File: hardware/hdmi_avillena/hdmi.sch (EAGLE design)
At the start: 5 parts

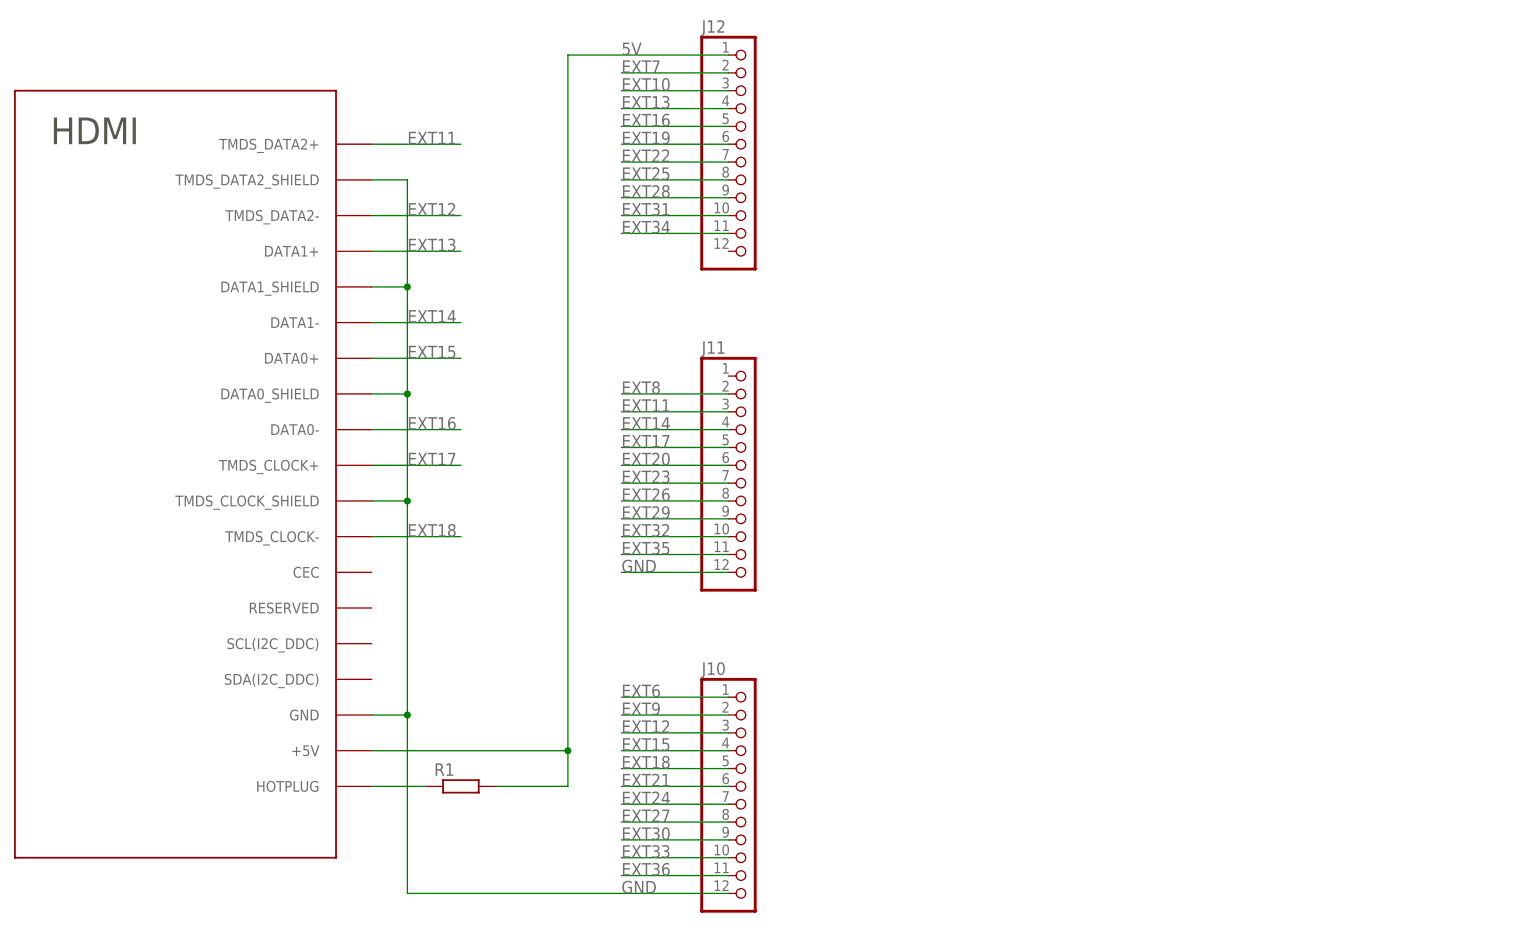
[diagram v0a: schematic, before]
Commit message: 
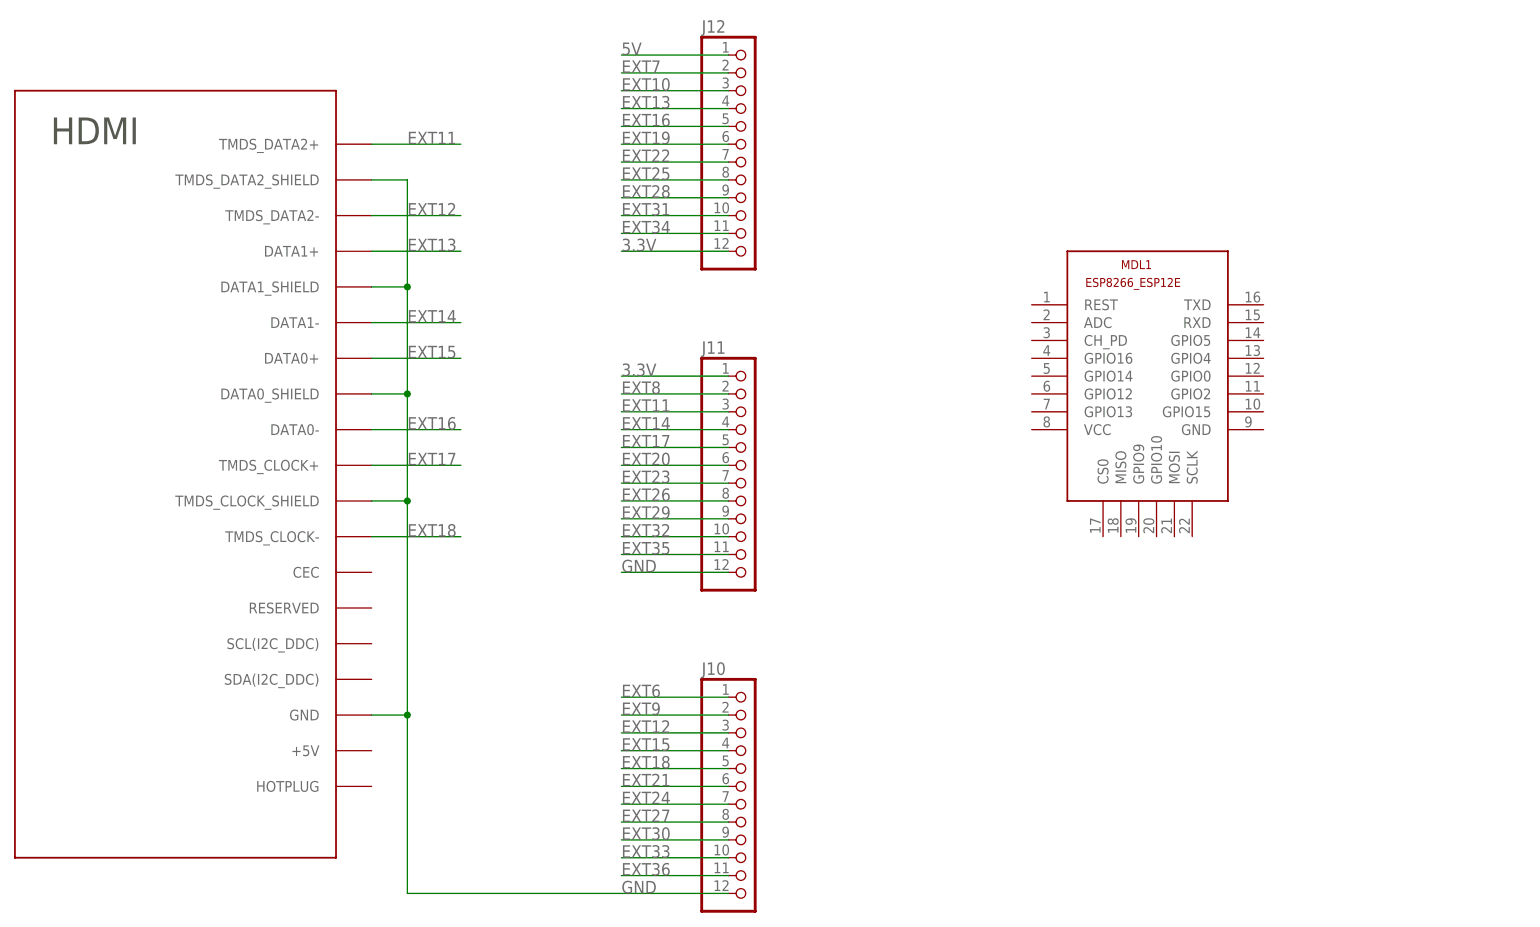
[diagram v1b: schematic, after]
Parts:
- removed R1: (no value), rcl:R-EU_0204/7
- added MDL1: (no value), ESP8266-ESP12E:ESP8266-12EESP8266-ESP12E
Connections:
- removed net N$2: R1.1, U$1.HOTPLUG
- new net 3.3V: J11.1, J12.12
- net 5V: no longer R1.2, U$1.+5V
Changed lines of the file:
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@@
 <part name="J10" library="pinhead" deviceset="PINHD-1X12" device=""/>
 <part name="U$1" library="00_cody" deviceset="HDMI" device=""/>
-<part name="R1" library="rcl" deviceset="R-EU_" device="0204/7"/>
+<part name="MDL1" library="ESP8266-ESP12E" deviceset="ESP8266-12E" device="ESP8266-ESP12E"/>
 </parts>
 <sheets>
@@
 <instance part="J10" gate="G$1" x="27.94" y="-2.54"/>
 <instance part="U$1" gate="G$1" x="-33.02" y="68.58"/>
-<instance part="R1" gate="G$1" x="-12.7" y="-2.54"/>
+<instance part="MDL1" gate="G$1" x="91.44" y="58.42"/>
 </instances>
 <busses>
@@
 </segment>
 </net>
-<net name="5V" class="0">
-<segment>
-<wire x1="2.54" y1="101.6" x2="25.4" y2="101.6" width="0.1524" layer="91"/>
-<label x="10.16" y="101.6" size="1.778" layer="95"/>
-<pinref part="J12" gate="G$1" pin="1"/>
-<pinref part="U$1" gate="G$1" pin="+5V"/>
-<wire x1="-25.4" y1="2.54" x2="2.54" y2="2.54" width="0.1524" layer="91"/>
-<wire x1="2.54" y1="2.54" x2="2.54" y2="101.6" width="0.1524" layer="91"/>
-<pinref part="R1" gate="G$1" pin="2"/>
-<wire x1="-7.62" y1="-2.54" x2="2.54" y2="-2.54" width="0.1524" layer="91"/>
-<wire x1="2.54" y1="-2.54" x2="2.54" y2="2.54" width="0.1524" layer="91"/>
-<junction x="2.54" y="2.54"/>
-</segment>
-</net>
 <net name="EXT6" class="0">
 <segment>
@@
 </segment>
 </net>
-<net name="N$2" class="0">
-<segment>
-<pinref part="U$1" gate="G$1" pin="HOTPLUG"/>
-<pinref part="R1" gate="G$1" pin="1"/>
-<wire x1="-25.4" y1="-2.54" x2="-17.78" y2="-2.54" width="0.1524" layer="91"/>
-</segment>
-</net>
+<net name="5V" class="0">
+<segment>
+<pinref part="J12" gate="G$1" pin="1"/>
+<wire x1="25.4" y1="101.6" x2="10.16" y2="101.6" width="0.1524" layer="91"/>
+<label x="10.16" y="101.6" size="1.778" layer="95"/>
+</segment>
+</net>
+<net name="3.3V" class="0">
+<segment>
+<pinref part="J11" gate="G$1" pin="1"/>
+<wire x1="25.4" y1="55.88" x2="10.16" y2="55.88" width="0.1524" layer="91"/>
+<label x="10.16" y="55.88" size="1.778" layer="95"/>
+</segment>
+<segment>
+<pinref part="J12" gate="G$1" pin="12"/>
+<wire x1="25.4" y1="73.66" x2="10.16" y2="73.66" width="0.1524" layer="91"/>
+<label x="10.16" y="73.66" size="1.778" layer="95"/>
+</segment>
+</net>

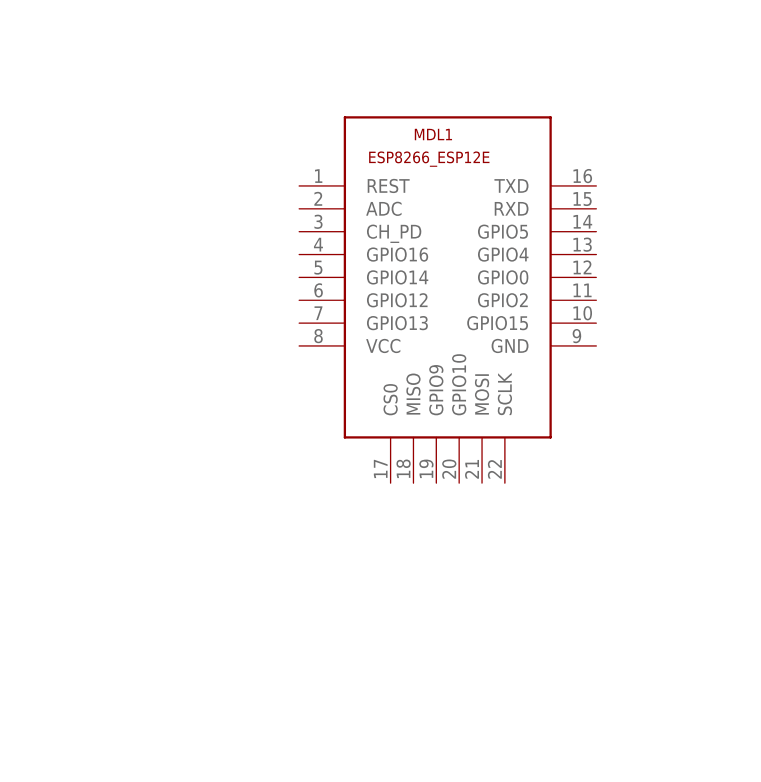
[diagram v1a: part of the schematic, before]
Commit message: 
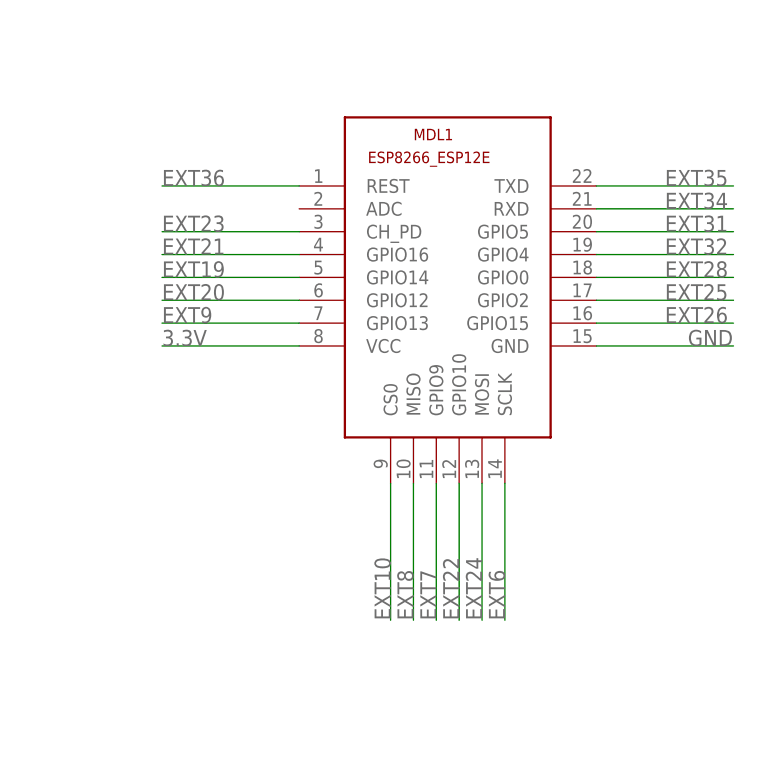
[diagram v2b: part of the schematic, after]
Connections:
- net 3.3V: now also MDL1.VCC
- net EXT10: now also MDL1.CS0
- net EXT19: now also MDL1.GPIO14
- net EXT20: now also MDL1.GPIO12
- net EXT21: now also MDL1.GPIO16
- net EXT22: now also MDL1.GPIO10
- net EXT23: now also MDL1.CH_PD
- net EXT24: now also MDL1.MOSI
- net EXT25: now also MDL1.GPIO2
- net EXT26: now also MDL1.GPIO15
- net EXT28: now also MDL1.GPIO0
- net EXT31: now also MDL1.GPIO5
- net EXT32: now also MDL1.GPIO4
- net EXT34: now also MDL1.RXD
- net EXT35: now also MDL1.TXD
- net EXT36: now also MDL1.REST
- net EXT6: now also MDL1.SCLK
- net EXT7: now also MDL1.GPIO9
- net EXT8: now also MDL1.MISO
- net EXT9: now also MDL1.GPIO13
- net GND: now also MDL1.GND

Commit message: 
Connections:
- removed net EXT36: J10.11, MDL1.REST
- net EXT33: now also MDL1.REST
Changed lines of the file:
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@@
 <grid distance="0.1" unitdist="inch" unit="inch" style="lines" multiple="1" display="no" altdistance="0.01" altunitdist="inch" altunit="inch"/>
 <layers>
-<layer number="1" name="Top" color="4" fill="1" visible="yes" active="no"/>
-<layer number="2" name="Route2" color="1" fill="3" visible="yes" active="no"/>
-<layer number="3" name="Route3" color="4" fill="3" visible="yes" active="no"/>
-<layer number="4" name="Route4" color="1" fill="4" visible="yes" active="no"/>
-<layer number="5" name="Route5" color="4" fill="4" visible="yes" active="no"/>
-<layer number="6" name="Route6" color="1" fill="8" visible="yes" active="no"/>
-<layer number="7" name="Route7" color="4" fill="8" visible="yes" active="no"/>
-<layer number="8" name="Route8" color="1" fill="2" visible="yes" active="no"/>
-<layer number="9" name="Route9" color="4" fill="2" visible="yes" active="no"/>
-<layer number="10" name="Route10" color="1" fill="7" visible="yes" active="no"/>
-<layer number="11" name="Route11" color="4" fill="7" visible="yes" active="no"/>
-<layer number="12" name="Route12" color="1" fill="5" visible="yes" active="no"/>
-<layer number="13" name="Route13" color="4" fill="5" visible="yes" active="no"/>
-<layer number="14" name="Route14" color="1" fill="6" visible="yes" active="no"/>
-<layer number="15" name="Route15" color="4" fill="6" visible="yes" active="no"/>
-<layer number="16" name="Bottom" color="1" fill="1" visible="yes" active="no"/>
-<layer number="17" name="Pads" color="2" fill="1" visible="yes" active="no"/>
-<layer number="18" name="Vias" color="2" fill="1" visible="yes" active="no"/>
-<layer number="19" name="Unrouted" color="6" fill="1" visible="yes" active="no"/>
-<layer number="20" name="Dimension" color="15" fill="1" visible="yes" active="no"/>
-<layer number="21" name="tPlace" color="7" fill="1" visible="yes" active="no"/>
-<layer number="22" name="bPlace" color="7" fill="1" visible="yes" active="no"/>
-<layer number="23" name="tOrigins" color="15" fill="1" visible="yes" active="no"/>
-<layer number="24" name="bOrigins" color="15" fill="1" visible="yes" active="no"/>
-<layer number="25" name="tNames" color="7" fill="1" visible="yes" active="no"/>
-<layer number="26" name="bNames" color="7" fill="1" visible="yes" active="no"/>
-<layer number="27" name="tValues" color="7" fill="1" visible="yes" active="no"/>
-<layer number="28" name="bValues" color="7" fill="1" visible="yes" active="no"/>
+<layer number="1" name="Top" color="4" fill="1" visible="no" active="no"/>
+<layer number="2" name="Route2" color="1" fill="3" visible="no" active="no"/>
+<layer number="3" name="Route3" color="4" fill="3" visible="no" active="no"/>
+<layer number="4" name="Route4" color="1" fill="4" visible="no" active="no"/>
+<layer number="5" name="Route5" color="4" fill="4" visible="no" active="no"/>
+<layer number="6" name="Route6" color="1" fill="8" visible="no" active="no"/>
+<layer number="7" name="Route7" color="4" fill="8" visible="no" active="no"/>
+<layer number="8" name="Route8" color="1" fill="2" visible="no" active="no"/>
+<layer number="9" name="Route9" color="4" fill="2" visible="no" active="no"/>
+<layer number="10" name="Route10" color="1" fill="7" visible="no" active="no"/>
+<layer number="11" name="Route11" color="4" fill="7" visible="no" active="no"/>
+<layer number="12" name="Route12" color="1" fill="5" visible="no" active="no"/>
+<layer number="13" name="Route13" color="4" fill="5" visible="no" active="no"/>
+<layer number="14" name="Route14" color="1" fill="6" visible="no" active="no"/>
+<layer number="15" name="Route15" color="4" fill="6" visible="no" active="no"/>
+<layer number="16" name="Bottom" color="1" fill="1" visible="no" active="no"/>
+<layer number="17" name="Pads" color="2" fill="1" visible="no" active="no"/>
+<layer number="18" name="Vias" color="2" fill="1" visible="no" active="no"/>
+<layer number="19" name="Unrouted" color="6" fill="1" visible="no" active="no"/>
+<layer number="20" name="Dimension" color="15" fill="1" visible="no" active="no"/>
+<layer number="21" name="tPlace" color="7" fill="1" visible="no" active="no"/>
+<layer number="22" name="bPlace" color="7" fill="1" visible="no" active="no"/>
+<layer number="23" name="tOrigins" color="15" fill="1" visible="no" active="no"/>
+<layer number="24" name="bOrigins" color="15" fill="1" visible="no" active="no"/>
+<layer number="25" name="tNames" color="7" fill="1" visible="no" active="no"/>
+<layer number="26" name="bNames" color="7" fill="1" visible="no" active="no"/>
+<layer number="27" name="tValues" color="7" fill="1" visible="no" active="no"/>
+<layer number="28" name="bValues" color="7" fill="1" visible="no" active="no"/>
 <layer number="29" name="tStop" color="7" fill="3" visible="no" active="no"/>
 <layer number="30" name="bStop" color="7" fill="6" visible="no" active="no"/>
@@
 <layer number="35" name="tGlue" color="7" fill="4" visible="no" active="no"/>
 <layer number="36" name="bGlue" color="7" fill="5" visible="no" active="no"/>
-<layer number="37" name="tTest" color="7" fill="1" visible="yes" active="no"/>
-<layer number="38" name="bTest" color="7" fill="1" visible="yes" active="no"/>
+<layer number="37" name="tTest" color="7" fill="1" visible="no" active="no"/>
+<layer number="38" name="bTest" color="7" fill="1" visible="no" active="no"/>
 <layer number="39" name="tKeepout" color="4" fill="11" visible="no" active="no"/>
 <layer number="40" name="bKeepout" color="1" fill="11" visible="no" active="no"/>
@@
 <layer number="44" name="Drills" color="7" fill="1" visible="no" active="no"/>
 <layer number="45" name="Holes" color="7" fill="1" visible="no" active="no"/>
-<layer number="46" name="Milling" color="3" fill="1" visible="yes" active="no"/>
-<layer number="47" name="Measures" color="7" fill="1" visible="yes" active="no"/>
-<layer number="48" name="Document" color="7" fill="1" visible="yes" active="no"/>
-<layer number="49" name="Reference" color="7" fill="1" visible="yes" active="no"/>
-<layer number="50" name="dxf" color="7" fill="1" visible="yes" active="no"/>
-<layer number="51" name="tDocu" color="7" fill="1" visible="yes" active="no"/>
-<layer number="52" name="bDocu" color="7" fill="1" visible="yes" active="no"/>
-<layer number="53" name="tGND_GNDA" color="7" fill="1" visible="yes" active="no"/>
-<layer number="54" name="bGND_GNDA" color="7" fill="1" visible="yes" active="no"/>
-<layer number="56" name="wert" color="7" fill="1" visible="yes" active="no"/>
-<layer number="57" name="tCAD" color="7" fill="1" visible="yes" active="no"/>
+<layer number="46" name="Milling" color="3" fill="1" visible="no" active="no"/>
+<layer number="47" name="Measures" color="7" fill="1" visible="no" active="no"/>
+<layer number="48" name="Document" color="7" fill="1" visible="no" active="no"/>
+<layer number="49" name="Reference" color="7" fill="1" visible="no" active="no"/>
+<layer number="50" name="dxf" color="7" fill="1" visible="no" active="no"/>
+<layer number="51" name="tDocu" color="7" fill="1" visible="no" active="no"/>
+<layer number="52" name="bDocu" color="7" fill="1" visible="no" active="no"/>
+<layer number="53" name="tGND_GNDA" color="7" fill="1" visible="no" active="no"/>
+<layer number="54" name="bGND_GNDA" color="7" fill="1" visible="no" active="no"/>
+<layer number="56" name="wert" color="7" fill="1" visible="no" active="no"/>
+<layer number="57" name="tCAD" color="7" fill="1" visible="no" active="no"/>
 <layer number="90" name="Modules" color="7" fill="1" visible="no" active="yes"/>
 <layer number="91" name="Nets" color="2" fill="1" visible="yes" active="yes"/>
@@
 <pinref part="J10" gate="G$1" pin="10"/>
 </segment>
+<segment>
+<wire x1="53.34" y1="66.04" x2="68.58" y2="66.04" width="0.1524" layer="91"/>
+<label x="53.34" y="66.04" size="1.778" layer="95"/>
+<pinref part="MDL1" gate="G$1" pin="REST"/>
+</segment>
 </net>
 <net name="EXT34" class="0">
@@
 </segment>
 </net>
-<net name="EXT36" class="0">
-<segment>
-<wire x1="10.16" y1="-15.24" x2="25.4" y2="-15.24" width="0.1524" layer="91"/>
-<label x="10.16" y="-15.24" size="1.778" layer="95"/>
-<pinref part="J10" gate="G$1" pin="11"/>
-</segment>
-<segment>
-<wire x1="53.34" y1="66.04" x2="68.58" y2="66.04" width="0.1524" layer="91"/>
-<label x="53.34" y="66.04" size="1.778" layer="95"/>
-<pinref part="MDL1" gate="G$1" pin="REST"/>
-</segment>
-</net>
